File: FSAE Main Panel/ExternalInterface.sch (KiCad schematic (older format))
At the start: 17 parts, among them J201 USB Micro B, J202 Cortex_Debug, J203 Conn_01x04, J204 TE_84953-6_FPC, SW1 B3W-1020, SW2 B3W-1020

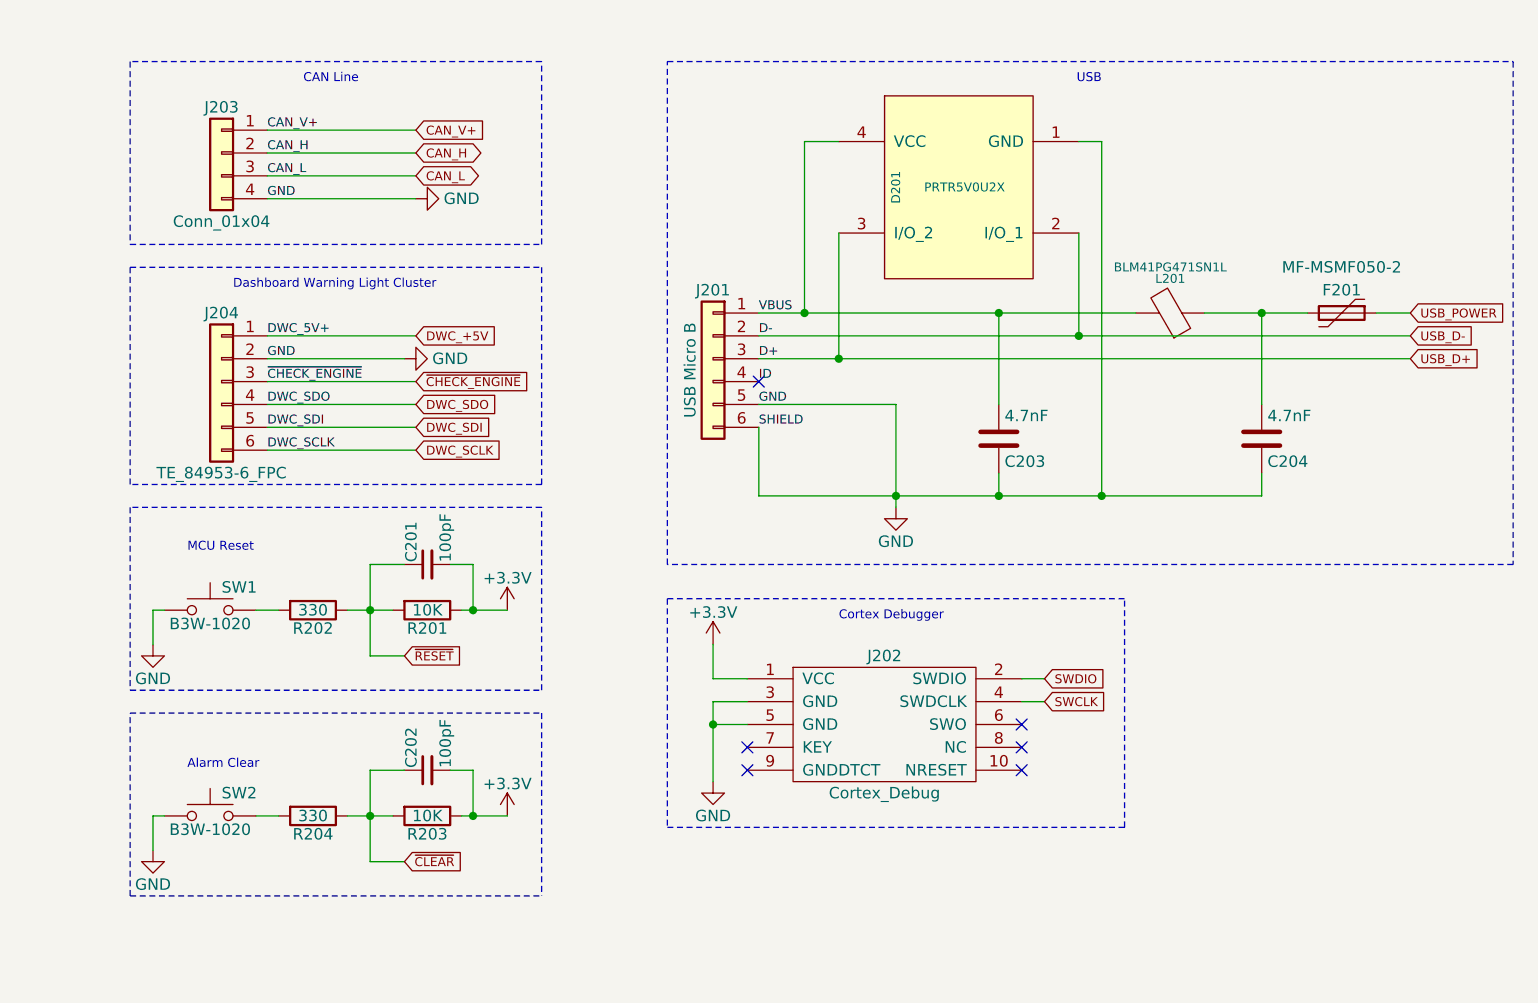
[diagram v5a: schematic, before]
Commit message: Major Revision
Deleted a ton of routes, Sorry Gary.
Changed all LEDs to 1206s for better brightness
Added a lot of local net names for easier routing
Flipped J203 for better routing
Expanded board outline to fit final dashboard cutout
Added half of the Mounting Holes
Realigned RPM strip
Added Linear Reg Load Resistors to meet minimum current specs
Changed Aux load Linear Regulators to a better one
Added Separate Linear Reg for the DWC
Tuned the CAN Bus differential Pair Lines for equal length
Added decoupling capacitors at a few locations
Rerouted Power traces to be shorter and cleaner
Set up keep out zones for CAN bus interference shielding.
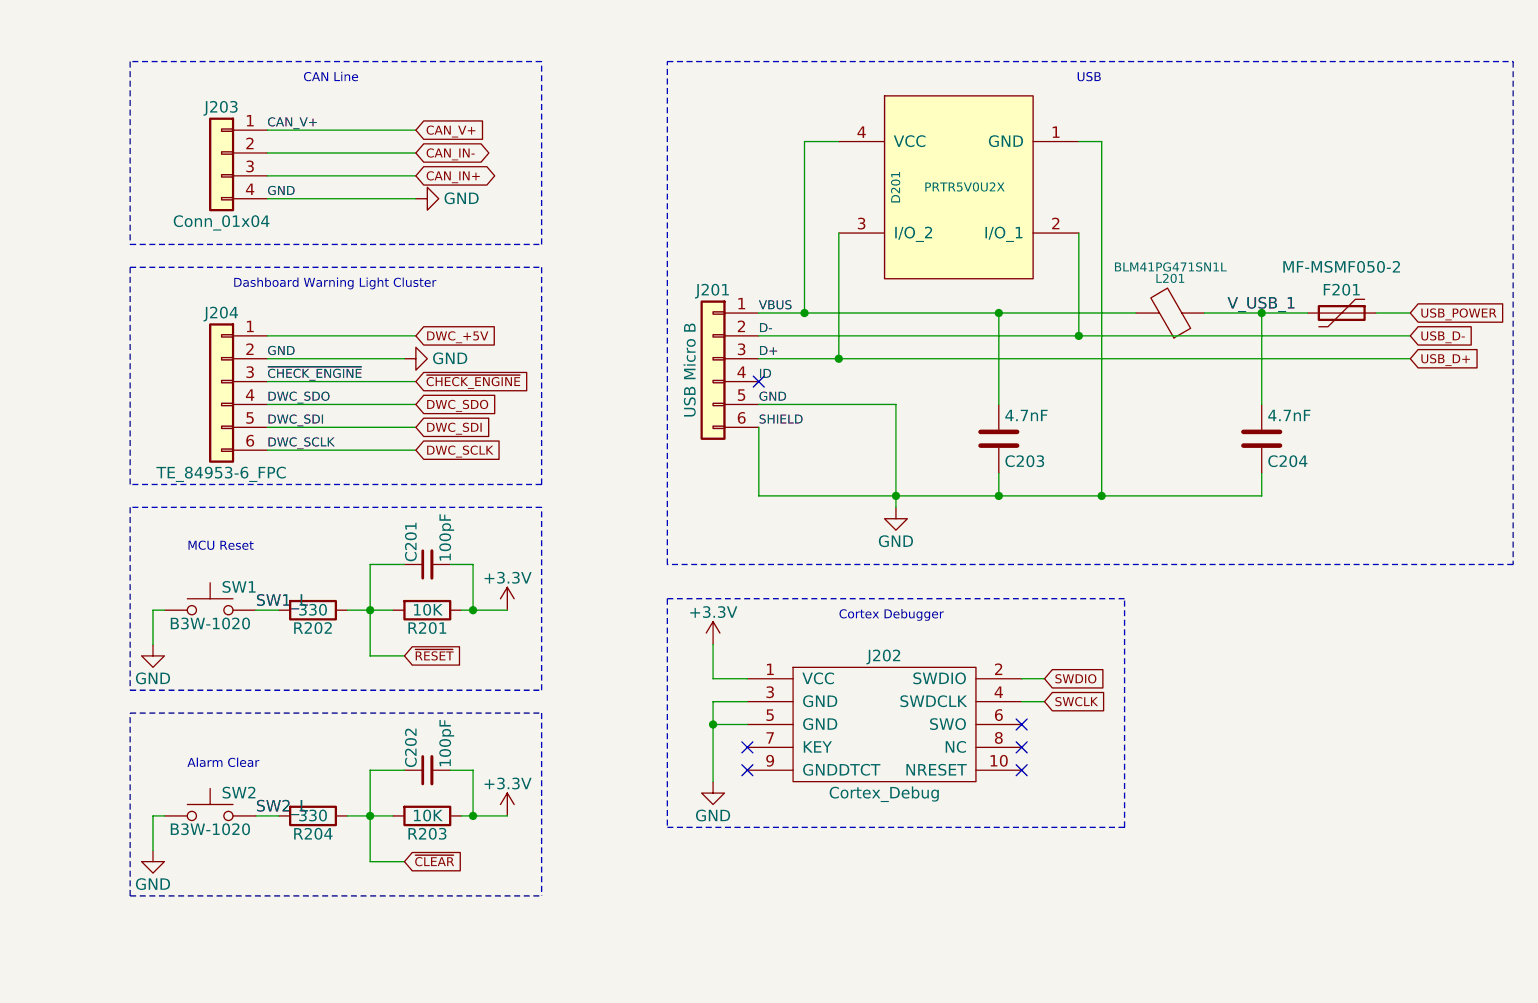
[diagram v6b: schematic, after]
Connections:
- net SW1_L: now reaches R202.2, SW1.2
- net SW2_L: now reaches R204.2, SW2.2
- net V_USB_1: now reaches C204.2, F201.2, L201.1
- net CAN_H renamed CAN_IN-
- net CAN_L renamed CAN_IN+
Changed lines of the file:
@@
 Text Label 1250 1150 0    39   ~ 0
 CAN_V+
-Text Label 1250 1250 0    39   ~ 0
-CAN_H
-Text Label 1250 1350 0    39   ~ 0
-CAN_L
 Text Label 1250 1450 0    39   ~ 0
 GND
@@
 	0    -1   -1   0
 $EndComp
+Text GLabel 1900 1350 2    39   BiDi ~ 0
+CAN_IN+
 Text GLabel 1900 1250 2    39   BiDi ~ 0
-CAN_H
-Text GLabel 1900 1350 2    39   BiDi ~ 0
-CAN_L
+CAN_IN-
 $Comp
 L conn:Conn_01x06 J204
@@
 	0    -1   -1   0
 $EndComp
-Text Label 1250 2050 0    39   ~ 0
-DWC_5V+
 Text Label 1250 2150 0    39   ~ 0
 GND
@@
 Wire Notes Line
 	650  4500 2450 4500
+Text Label 5450 1950 0    50   ~ 0
+V_USB_1
+Text Label 1200 4150 0    50   ~ 0
+SW2_L
+Text Label 1200 3250 0    50   ~ 0
+SW1_L
 $EndSCHEMATC

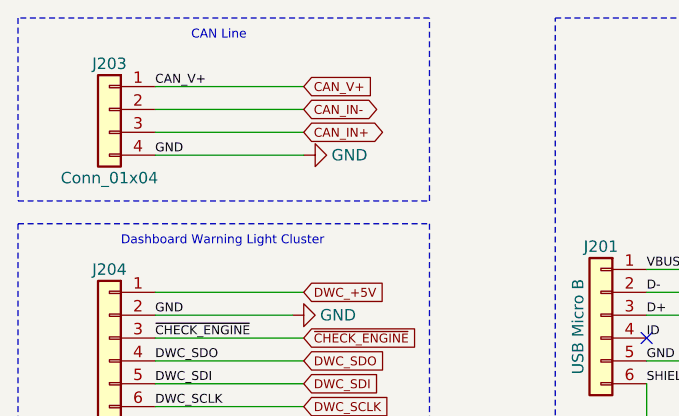
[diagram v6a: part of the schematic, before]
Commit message: Power Supply Changes Again
Shrunk some 5V layout by switching LM7805's for their SOT223 packages but with very careful top copper considerations for thermal management.
Shrunk the Right side by 12mm for more clearance near ignition button.
Fixed Shift Register clock signal routing.
Changed shift order to be 7 segment first for easiler routing.
Added Mounting Holes.
TODO: Figure out Top layer 7 segment placement.
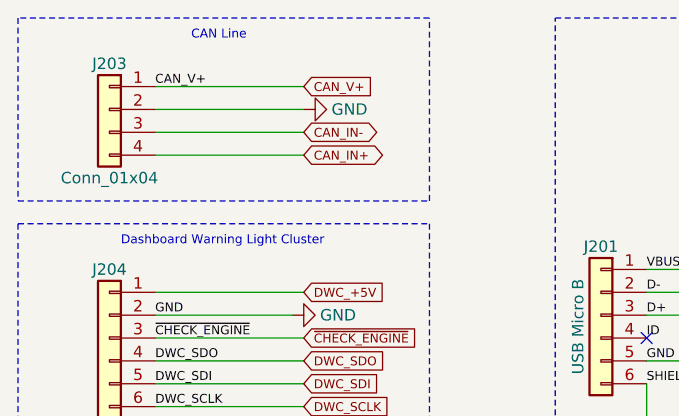
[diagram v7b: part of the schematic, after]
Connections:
- net CAN_IN+: now also J203.4 (Pin_4); no longer J203.3 (Pin_3)
- net CAN_IN-: now also J203.3 (Pin_3); no longer J203.2 (Pin_2)
- net GND: now also J203.2 (Pin_2); no longer J203.4 (Pin_4)
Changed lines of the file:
@@
 Text Label 1250 1150 0    39   ~ 0
 CAN_V+
-Text Label 1250 1450 0    39   ~ 0
-GND
 Text GLabel 1900 1150 2    39   Input ~ 0
 CAN_V+
@@
 L power:GND #PWR0204
 U 1 1 5BE24FFA
-P 1900 1450
-F 0 "#PWR0204" H 1900 1200 50  0001 C CNN
-F 1 "GND" V 1900 1250 50  0000 C CNN
-F 2 "" H 1900 1450 50  0001 C CNN
-F 3 "" H 1900 1450 50  0001 C CNN
-	1    1900 1450
+P 1900 1250
+F 0 "#PWR0204" H 1900 1000 50  0001 C CNN
+F 1 "GND" V 1900 1050 50  0000 C CNN
+F 2 "" H 1900 1250 50  0001 C CNN
+F 3 "" H 1900 1250 50  0001 C CNN
+	1    1900 1250
 	0    -1   -1   0
 $EndComp
+Text GLabel 1900 1450 2    39   BiDi ~ 0
+CAN_IN+
 Text GLabel 1900 1350 2    39   BiDi ~ 0
-CAN_IN+
-Text GLabel 1900 1250 2    39   BiDi ~ 0
 CAN_IN-
 $Comp

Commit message: More Routing
Fixed Tactile Switch Footprints
More routing
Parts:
- removed SW2: B3W-1020, Buttons_Switches_THT:SW_TH_Tactile_Omron_B3F-10xx, symbol switches:SW_Push
- added SW2: B3W-1020, Buttons_Switches_THT:SW_TH_Tactile_Omron_B3F-10xx, symbol Omron:B3W-1000
- SW1: symbol switches:SW_Push -> Omron:B3W-1000
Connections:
- net GND: now also SW1.2, SW2.1, SW2.2
- net SW1_L: now also SW1.3, SW1.4; no longer SW1.2
- net SW2_L: now also SW2.3, SW2.4
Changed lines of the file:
@@
 Dashboard Warning Light Cluster
 $Comp
-L switches:SW_Push SW1
+L Omron:B3W-1000 SW1
 U 1 1 5BE9B978
 P 1000 3250
@@
 F 4 "Omron" H 1000 3250 60  0001 C CNN "Manufacturer"
 	1    1000 3250
-	1    0    0    -1
+	0    1    1    0
 $EndComp
 Text Notes 900  3000 0    39   ~ 0
 MCU Reset
-$Comp
-L switches:SW_Push SW2
-U 1 1 5BE9BA9C
-P 1000 4150
-F 0 "SW2" H 1050 4250 50  0000 L CNN
-F 1 "B3W-1020" H 1000 4090 50  0000 C CNN
-F 2 "Buttons_Switches_THT:SW_TH_Tactile_Omron_B3F-10xx" H 1000 4350 50  0001 C CNN
-F 3 "https://www.mouser.com/datasheet/2/307/en-b3w-779787.pdf" H 1000 4350 50  0001 C CNN
-F 4 "Omron" H 1000 4150 60  0001 C CNN "Manufacturer"
-	1    1000 4150
-	1    0    0    -1
-$EndComp
 Text Notes 900  3950 0    39   ~ 0
 Alarm Clear
@@
 	750  4150 750  4300
 Wire Wire Line
-	800  3250 750  3250
-Wire Wire Line
 	750  3250 750  3400
 Wire Wire Line
@@
 Text Label 1200 3250 0    50   ~ 0
 SW1_L
+$Comp
+L Omron:B3W-1000 SW2
+U 1 1 5C8459CA
+P 1000 4150
+F 0 "SW2" H 1050 4250 50  0000 L CNN
+F 1 "B3W-1020" H 1000 4090 50  0000 C CNN
+F 2 "Buttons_Switches_THT:SW_TH_Tactile_Omron_B3F-10xx" H 1000 4350 50  0001 C CNN
+F 3 "https://www.mouser.com/datasheet/2/307/en-b3w-779787.pdf" H 1000 4350 50  0001 C CNN
+F 4 "Omron" H 1000 4150 60  0001 C CNN "Manufacturer"
+	1    1000 4150
+	0    1    1    0
+$EndComp
+Wire Wire Line
+	950  3950 800  3950
+Wire Wire Line
+	800  3950 800  4150
+Wire Wire Line
+	800  4150 800  4350
+Wire Wire Line
+	800  4350 950  4350
+Connection ~ 800  4150
+Wire Wire Line
+	1150 4350 1200 4350
+Wire Wire Line
+	1200 4350 1200 4150
+Wire Wire Line
+	1200 4150 1200 3950
+Wire Wire Line
+	1200 3950 1150 3950
+Connection ~ 1200 4150
+Wire Wire Line
+	1150 3050 1200 3050
+Wire Wire Line
+	1200 3050 1200 3250
+Wire Wire Line
+	1200 3250 1200 3450
+Wire Wire Line
+	1200 3450 1150 3450
+Connection ~ 1200 3250
+Wire Wire Line
+	950  3050 900  3050
+Wire Wire Line
+	900  3050 900  3250
+Wire Wire Line
+	900  3450 950  3450
+Wire Wire Line
+	750  3250 900  3250
+Connection ~ 900  3250
+Wire Wire Line
+	900  3250 900  3450
 $EndSCHEMATC
